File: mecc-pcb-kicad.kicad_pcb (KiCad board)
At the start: 2 copper layers, 230.1 x 130 mm, 73 parts, among them J1 VESC Term, J2 STM SIGS, J2 VBatt -> 5V, J3 Wave_Gauge, J4 5V -> 3.3V, J5 PDQE15-Q48-D24-D, J6 VESC IN, J7 UI BUS, J8 Torq_SENS, Q1 NMOS, Q2 NMOS, Q3 PMOS, Q4 PMOS, Q5 NMOS, SW1 Reset, U1 SEN-16407, U2 SN74HCS09QPWRQ1, U3 SN74LVC1G139DCUR

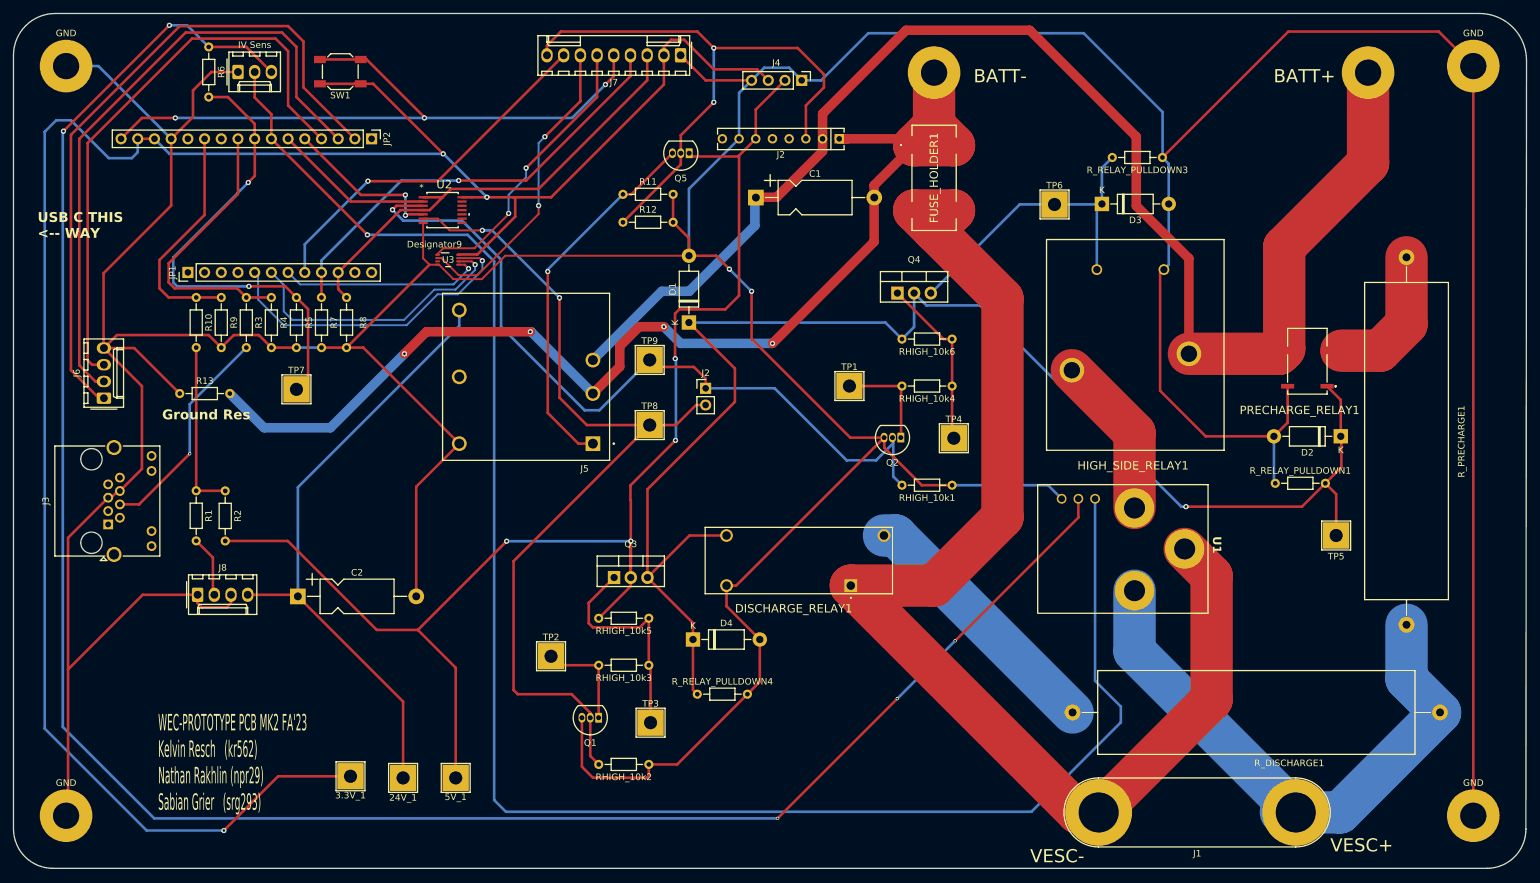
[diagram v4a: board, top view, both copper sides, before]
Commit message: Implemented Becca's comments. Board should be ready for final review
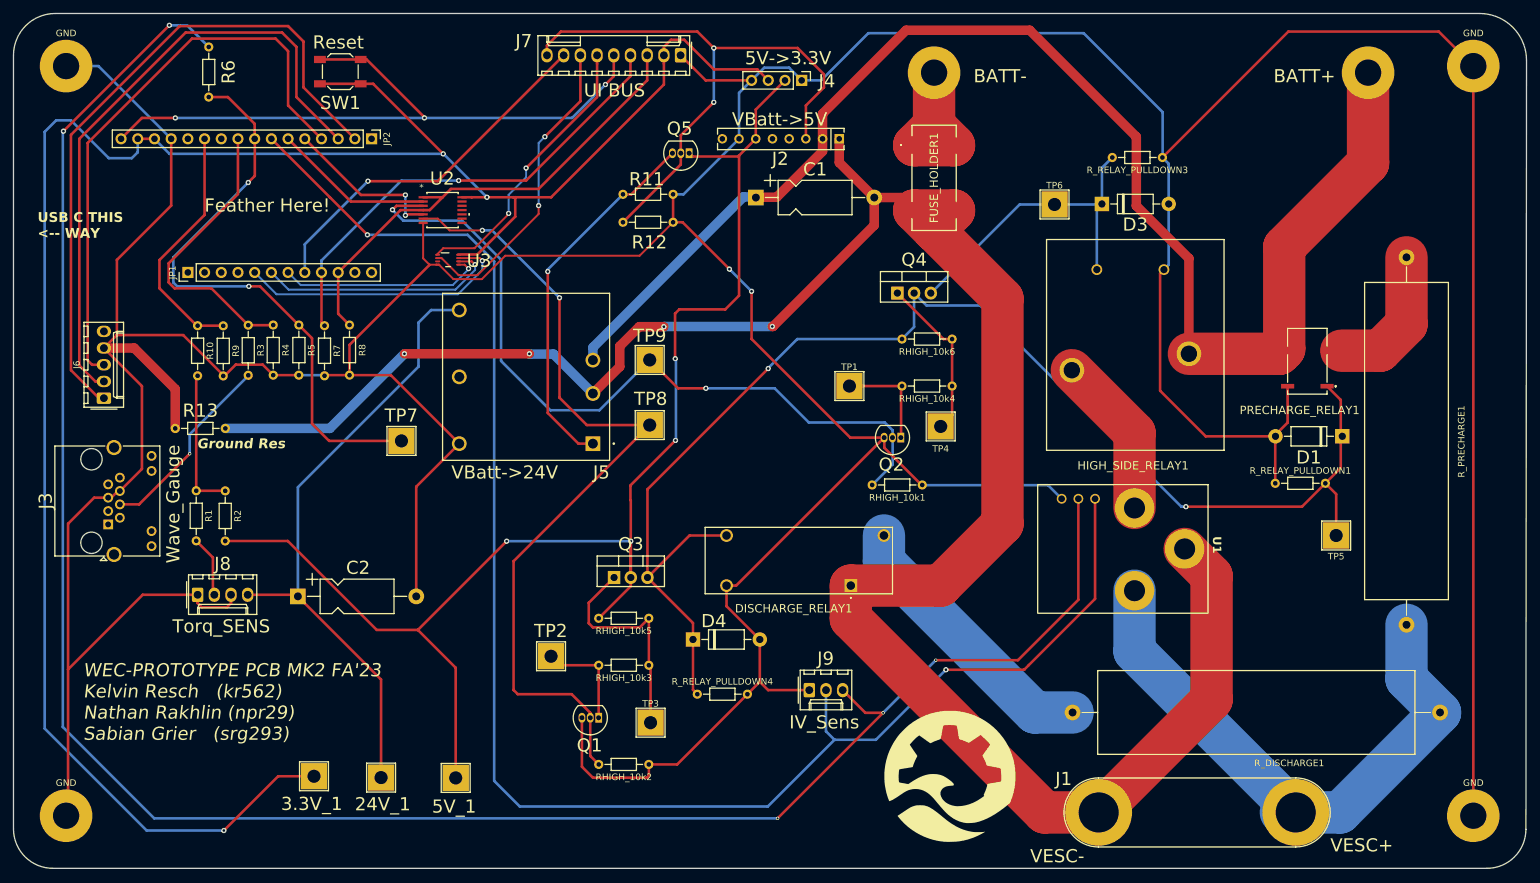
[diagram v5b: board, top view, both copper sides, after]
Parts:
- removed D2: 1N4007, Diode_THT:D_DO-41_SOD81_P10.16mm_Horizontal
- removed IV Sens: IV Sens, Connector_Molex:Molex_KK-254_AE-6410-03A_1x03_P2.54mm_Vertical
- removed the J2 at (175.3, 137.0)
- added G***: LOGO, LOGO, F.Cu at (212.4, 196.0)
- added J9: IV_Sens, Connector_Molex:Molex_KK-254_AE-6410-03A_1x03_P2.54mm_Vertical, F.Cu at (191.0, 182.9)
- J6: footprint Connector_Molex:Molex_KK-254_AE-6410-04A_1x04_P2.54mm_Vertical -> Connector_Molex:Molex_KK-254_AE-6410-05A_1x05_P2.54mm_Vertical
- moved D1 100.9 mm to (272.1, 144.3), turned to 180 degrees
- moved TP7 17.8 mm to (129.0, 145.0)
- moved 3.3V_1 5.55 mm to (115.7, 196.0)
- moved R13 5.34 mm to (94.6, 143.1)
- moved RHIGH_10k1 4.54 mm to (208.2, 151.7)
- moved R9 4.32 mm to (101.9, 127.5)
- moved R7 4.31 mm to (117.3, 135.1)
- moved R10 4.30 mm to (98.0, 135.1)
- moved R3 4.22 mm to (105.7, 127.4)
- moved R8 4.21 mm to (121.1, 135.0)
- moved R5 4.21 mm to (113.4, 135.0)
- moved R4 4.20 mm to (109.5, 135.0)
- moved 24V_1 3.35 mm to (125.9, 196.2)
- moved TP4 2.69 mm to (211.0, 142.8)
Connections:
- net HIGH_SIDE_STM renamed HIGH_SIDE_ANDOUT
- net PRE_LOW_DIS renamed PRE_DIS
- net PRE_LOW_DIS_STM renamed PRE_DIS_ANDOUT
- C1 pad 2: BATT_NEG -> VESC_NEG
- J2 pad 1: BATT_NEG -> VESC_NEG
- J5 pad 2: BATT_NEG -> VESC_NEG
- R13 pad 2: BATT_NEG -> VESC_NEG
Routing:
- net BATT_NEG: track 175.5 -> 21.7 mm, vias 4 -> 0
- net VESC_NEG: track 190.8 -> 334.9 mm, vias 0 -> 4
- net BATT_CURR_SENSOR: track 272.0 -> 250.0 mm, vias 1 -> 2
- net PRE_DIS: track 227.0 -> 208.0 mm, vias 1 -> 2
- net /A4: track 73.1 -> 90.2 mm
- net GND: track 900.6 -> 890.5 mm
- net PRE_DIS_ANDOUT: track 136.5 -> 126.7 mm
- net Torq_SW_Mode_2: track 43.1 -> 37.0 mm
- net Torq_SW_Mode_1: track 48.8 -> 42.8 mm
- net +3.3V: track 324.3 -> 318.7 mm
- net ADVANCE_BUTTON_RED: track 67.4 -> 71.9 mm
- net IO_ESTOP: track 70.2 -> 74.6 mm
- net Net-(R1-Pad2): track 26.2 -> 22.0 mm
- net WAVE_GAUGE: track 33.5 -> 29.4 mm
- net BATT_V_SENSOR: track 313.9 -> 317.7 mm
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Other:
- board text added: "5V->3.3V"
- board text added: "Feather Here!"
- board text added: "IV_Sens"
- board text added: "Reset"
- board text added: "Torq_SENS"
- board text added: "UI BUS"
- board text added: "VBatt->24V"
- board text added: "VBatt->5V"
- board text added: "VESC IN"
- board text added: "Wave_Gauge"

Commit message: Added Gerber files
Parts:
- added GND_1: TestPoint, TestPoint:TestPoint_THTPad_4.0x4.0mm_Drill2.0mm, F.Cu at (174.7, 121.2)
- added SW2: Reset, Button_Switch_SMD:SW_SPST_SKQG_WithoutStem, F.Cu at (132.0, 89.2)
- added TP10: TestPoint, TestPoint:TestPoint_THTPad_4.0x4.0mm_Drill2.0mm, F.Cu at (103.6, 150.8)
- added TP11: TestPoint, TestPoint:TestPoint_THTPad_4.0x4.0mm_Drill2.0mm, F.Cu at (109.2, 150.7)
- added TP12: TestPoint, TestPoint:TestPoint_THTPad_4.0x4.0mm_Drill2.0mm, F.Cu at (114.8, 150.7)
- added TP13: TestPoint, TestPoint:TestPoint_THTPad_4.0x4.0mm_Drill2.0mm, F.Cu at (90.8, 140.0)
- added TP14: TestPoint, TestPoint:TestPoint_THTPad_4.0x4.0mm_Drill2.0mm, F.Cu at (162.3, 118.5)
- added TP15: TestPoint, TestPoint:TestPoint_THTPad_4.0x4.0mm_Drill2.0mm, F.Cu at (128.8, 150.6)
- added TP16: TestPoint, TestPoint:TestPoint_THTPad_4.0x4.0mm_Drill2.0mm, F.Cu at (123.1, 150.7)
- added TP17: TestPoint, TestPoint:TestPoint_THTPad_4.0x4.0mm_Drill2.0mm, F.Cu at (143.0, 86.3)
- added TP18: TestPoint, TestPoint:TestPoint_THTPad_4.0x4.0mm_Drill2.0mm, F.Cu at (147.6, 154.2)
- added TP9: TestPoint, TestPoint:TestPoint_THTPad_4.0x4.0mm_Drill2.0mm, F.Cu at (123.3, 157.0)
- moved TP7 43.9 mm to (172.0, 154.0)
- moved R2 11.7 mm to (108.2, 162.7), turned to 0 degrees
- moved ? 10.0 mm to (266.0, 89.0)
- moved C1 7.07 mm to (182.0, 115.0)
- moved R_DISCHARGE1 5.11 mm to (225.9, 186.2)
- moved SW1 2.70 mm to (117.0, 88.8)
- moved R1 2.62 mm to (98.2, 162.8), turned to 0 degrees
- moved J2 1.94 mm to (195.6, 101.0)
- moved R6 0.96 mm to (100.0, 86.0)
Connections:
- JP2 pad 1: /BOOT0 -> BOOT0
- TP7 pad 1: /A4 -> PRE_DIS
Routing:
- net ADVANCE_BUTTON_RED: track 71.9 -> 104.1 mm
- net IO_ESTOP: track 74.6 -> 99.9 mm
- net /A3: track 44.8 -> 69.8 mm
- net /A1: track 37.6 -> 61.8 mm
- net +3.3V: track 318.7 -> 340.4 mm
- net GND: track 890.5 -> 908.5 mm
- net BOOT0: track 0.00 -> 17.2 mm, vias 0 -> 2
- net VESC_NEG: track 334.9 -> 349.8 mm
- net Net-(R1-Pad2): track 22.0 -> 36.4 mm
- net Net-(J5-CTRL): track 56.9 -> 69.2 mm
- net +5V: track 208.9 -> 196.7 mm
- net DCDC_SW: track 90.3 -> 100.4 mm
- net /A4: track 90.2 -> 83.2 mm
- net +24V: track 97.2 -> 103.5 mm
- net PRE_DIS: track 208.0 -> 213.6 mm
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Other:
- board text added: "(kr562) (npr29) (srg293)"
- board text added: "BOOT"
- board text added: "WEC-PROTOTYPE PCB MK2 FA'23 Kelvin Resch Nathan Rakhlin Sabian Grier"
- board text removed: "WEC-PROTOTYPE PCB MK2 FA'23 Kelvin Resch (kr562) Nathan Rakhlin (npr29) Sabian Grier (srg293)"
